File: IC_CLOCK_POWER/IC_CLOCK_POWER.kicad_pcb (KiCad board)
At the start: 2 copper layers, 25 parts, among them J1 JACK, J2 Conn_01x04_Pin, U1 LM317T, U2 L7805

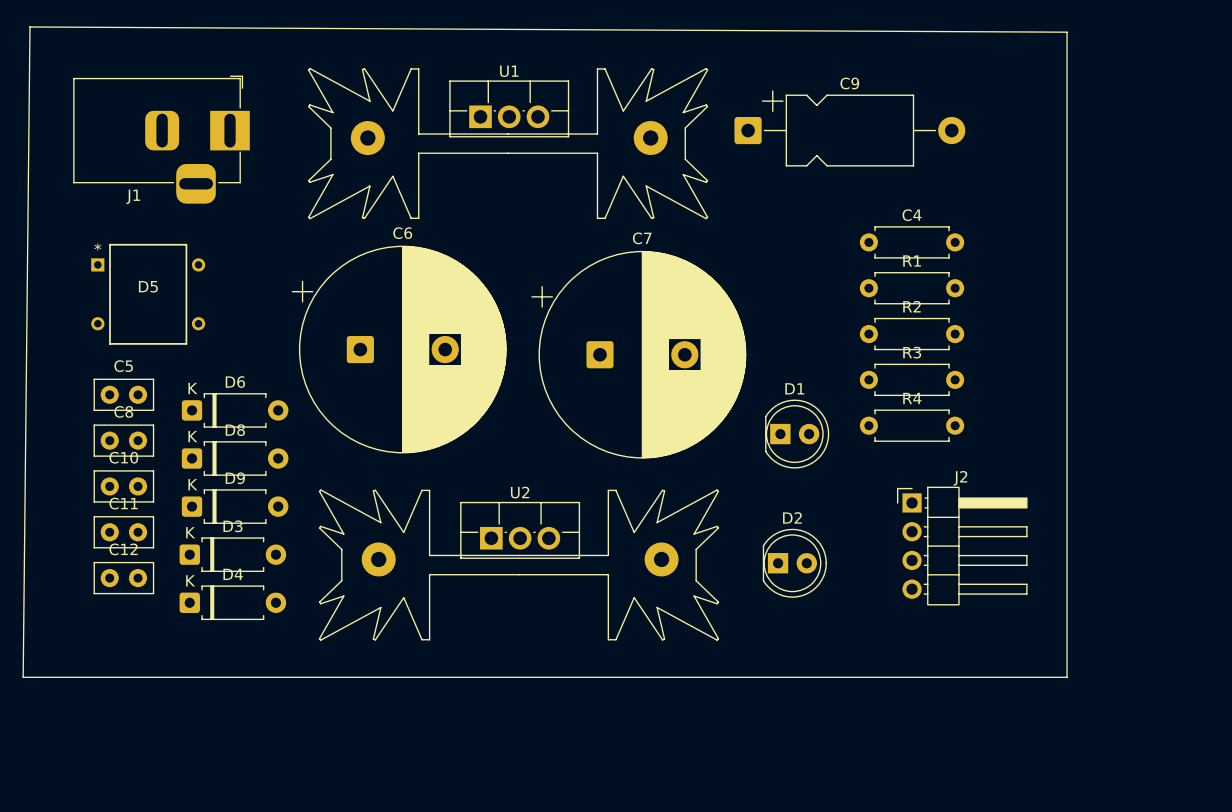
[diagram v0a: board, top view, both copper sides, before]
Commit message: Fixing schematic ..and footprints
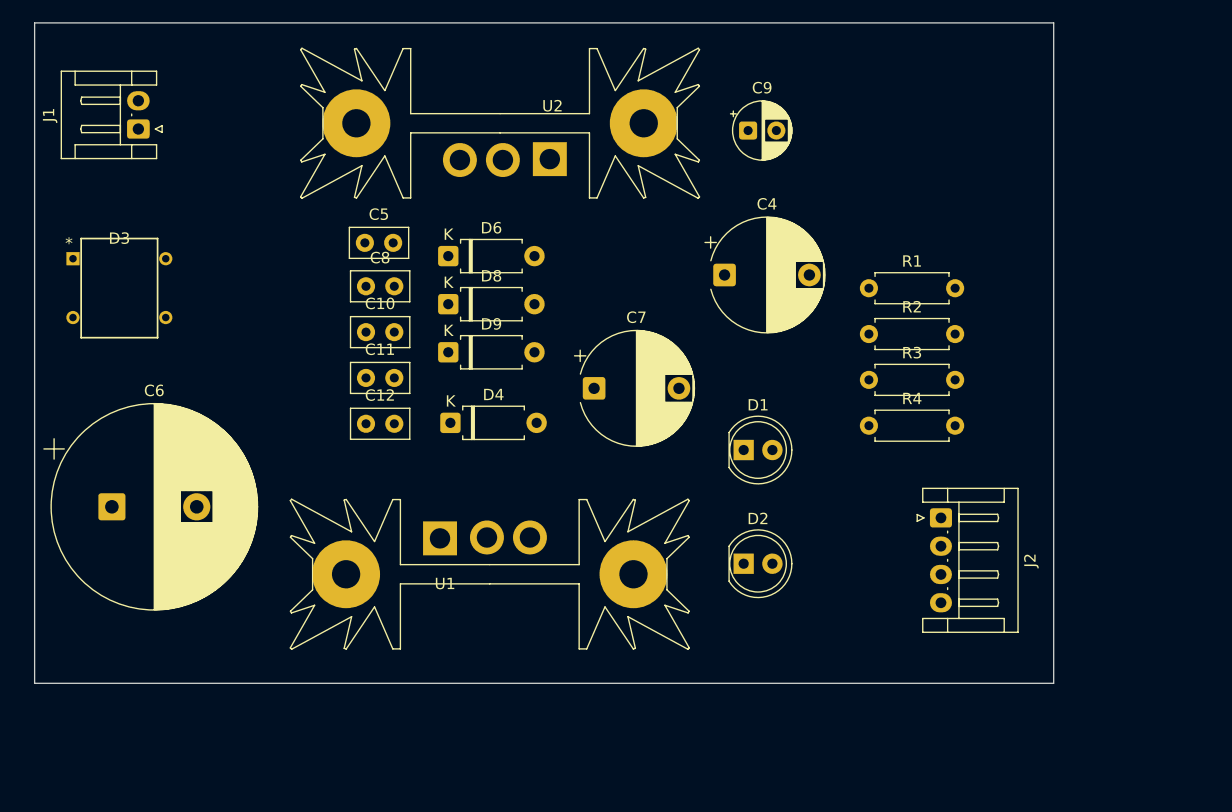
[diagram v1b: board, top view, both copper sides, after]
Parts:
- removed D5: DB107, IC_CLOCK:Bridge_Rectifier_4EDIP
- C10: value c=0.1u -> 0.1u
- C4: footprint Resistor_THT:R_Axial_DIN0207_L6.3mm_D2.5mm_P7.62mm_Horizontal -> Capacitor_THT:CP_Radial_D10.0mm_P7.50mm
- C7: value c=10m -> 10mF; footprint Capacitor_THT:CP_Radial_D18.0mm_P7.50mm -> Capacitor_THT:CP_Radial_D10.0mm_P7.50mm
- C9: footprint Capacitor_THT:CP_Axial_L11.0mm_D6.0mm_P18.00mm_Horizontal -> Capacitor_THT:CP_Radial_D5.0mm_P2.50mm
- D3: value 1N4002 -> Bridge_Rectifiers; footprint Diode_THT:D_A-405_P7.62mm_Horizontal -> IC_CLOCK:Bridge_Rectifier_4EDIP
- J1: value JACK -> Conn_01x02_Pin; footprint Connector_BarrelJack:BarrelJack_Horizontal -> Connector_JST:JST_EH_S2B-EH_1x02_P2.50mm_Horizontal
- J2: footprint Connector_PinHeader_2.54mm:PinHeader_1x04_P2.54mm_Horizontal -> Connector_JST:JST_EH_S4B-EH_1x04_P2.50mm_Horizontal
- R2: value r=1k -> 1k
- R4: value r=240 -> 240
- U1: value LM317T -> LM7805_TO220_HEAT_SINK; footprint Package_TO_SOT_THT:TO-220F-3_HEATSINK_Vertical -> IC_CLOCK:TO-220-HEADSINK-35X12
- U2: value L7805 -> LM317T; footprint Package_TO_SOT_THT:TO-220F-3_HEATSINK_Vertical -> IC_CLOCK:TO-220-HEADSINK-35X12
- moved U2 38.7 mm to (139.3, 92.9), turned to 180 degrees
- moved U1 38.4 mm to (137.9, 132.7)
- moved D4 28.0 mm to (134.7, 119.3)
- moved C11 26.4 mm to (127.2, 115.4)
- moved C10 26.4 mm to (127.2, 111.3)
- moved C8 26.4 mm to (127.2, 107.3)
- moved D6 26.4 mm to (134.5, 104.6)
- moved D8 26.4 mm to (134.5, 108.9)
- moved D9 26.4 mm to (134.5, 113.1)
- moved C12 26.4 mm to (127.2, 119.4)
- moved C5 26.2 mm to (127.1, 103.4)
- moved C6 26.0 mm to (104.7, 126.8)
- moved D3 24.5 mm to (105.4, 107.3)
- moved C4 13.1 mm to (158.9, 106.3)
- moved J1 8.10 mm to (107.1, 93.4), turned to 90 degrees
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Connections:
- C10 pad 1: -BATT -> GND
- C10 pad 2: Net-(D4-A) -> Net-(D3-+)
- C11 pad 1: -BATT -> GND
- C12 pad 1: -BATT -> GND
- C4 pad 1: Net-(D3-K) -> Net-(D4-K)
- C4 pad 2: -BATT -> GND
- C5 pad 2: -BATT -> GND
- C6 pad 1: Net-(D4-A) -> Net-(D3-+)
- C6 pad 2: -BATT -> GND
- C7 pad 1: Net-(D4-A) -> Net-(D3-+)
- C7 pad 2: -BATT -> GND
- C8 pad 2: -BATT -> GND
- C9 pad 2: -BATT -> GND
- D3 pad 1: Net-(D3-K) -> Net-(D3-+)
- D3 pad 2: +9v -> GND
- D4 pad 1: Net-(D3-K) -> Net-(D4-K)
- D4 pad 2: Net-(D4-A) -> Net-(D3-+)
- D8 pad 1: Net-(D3-K) -> Net-(D4-K)
- D9 pad 1: Net-(D4-A) -> Net-(D3-+)
- J1 pad 2: Net-(D5-Pad3) -> AC-GND
- J2 pad 1: -BATT -> GND
- R1 pad 1: -BATT -> GND
- R2 pad 1: -BATT -> GND
- R3 pad 2: -BATT -> GND
- U1 pad 1: Net-(D6-A) -> Net-(D4-K)
- U1 pad 2: +10V -> GND
- U1 pad 3: Net-(D4-A) -> +5V
- U1 pad 4: (no net) -> unconnected-(U1-HEADSINK-Pad4)
- U2 pad 1: Net-(D3-K) -> Net-(D6-A)
- U2 pad 2: -BATT -> +10V
- U2 pad 3: +5V -> Net-(D3-+)
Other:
- board outline added: 90.1 x 58.4 mm

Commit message: Update to files ...
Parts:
- moved C5 53.4 mm to (158.6, 146.6), turned to 90 degrees
- moved C10 47.4 mm to (173.0, 123.8), turned to 180 degrees
- moved C11 45.9 mm to (164.7, 141.9), turned to -90 degrees
- moved D9 43.3 mm to (177.2, 120.1), turned to 90 degrees
- moved C8 40.7 mm to (167.8, 104.5), turned to 90 degrees
- moved C12 38.1 mm to (164.2, 110.3), turned to 90 degrees
- moved D8 37.2 mm to (164.8, 130.4), turned to -90 degrees
- moved R1 34.6 mm to (148.4, 133.0), turned to -90 degrees
- moved D6 33.7 mm to (168.0, 107.6), turned to -90 degrees
- moved J1 32.7 mm to (109.0, 126.0)
- moved C4 31.6 mm to (153.0, 137.3)
- moved D4 31.3 mm to (164.9, 127.6), turned to 90 degrees
- moved C6 26.9 mm to (131.5, 124.9)
- moved D2 26.6 mm to (148.9, 107.9), turned to 90 degrees
- moved C9 26.3 mm to (172.1, 117.4), turned to -90 degrees
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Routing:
- net +10V: track 0.00 -> 89.3 mm
- net Net-(D3-+): track 0.00 -> 84.4 mm
- net 12VAC: track 0.00 -> 79.8 mm
- net +5V: track 0.00 -> 78.0 mm
- net Net-(D6-A): track 0.00 -> 59.3 mm
- net Net-(D4-K): track 0.00 -> 41.1 mm
- net AC-GND: track 0.00 -> 6.90 mm
- net Net-(D1-K): track 0.00 -> 4.12 mm
- net Net-(D2-K): track 0.00 -> 4.01 mm
- added copper zone on B.Cu, net GND
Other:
- board size 90.1 x 58.4 mm -> 100 x 50 mm
